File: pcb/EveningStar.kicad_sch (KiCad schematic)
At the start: 0 parts

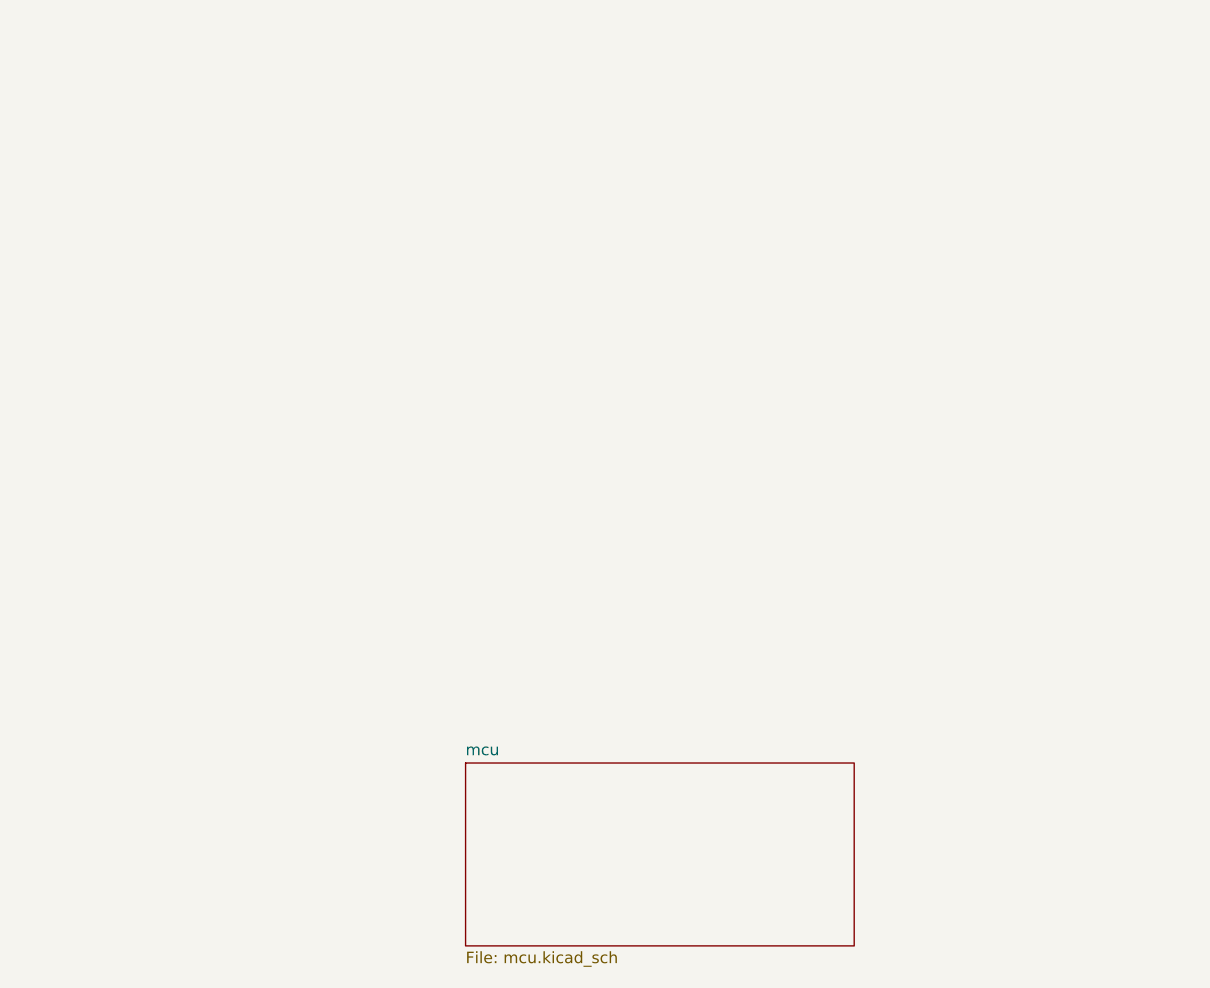
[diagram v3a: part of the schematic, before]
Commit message: feat: add W5500 ethernet controller
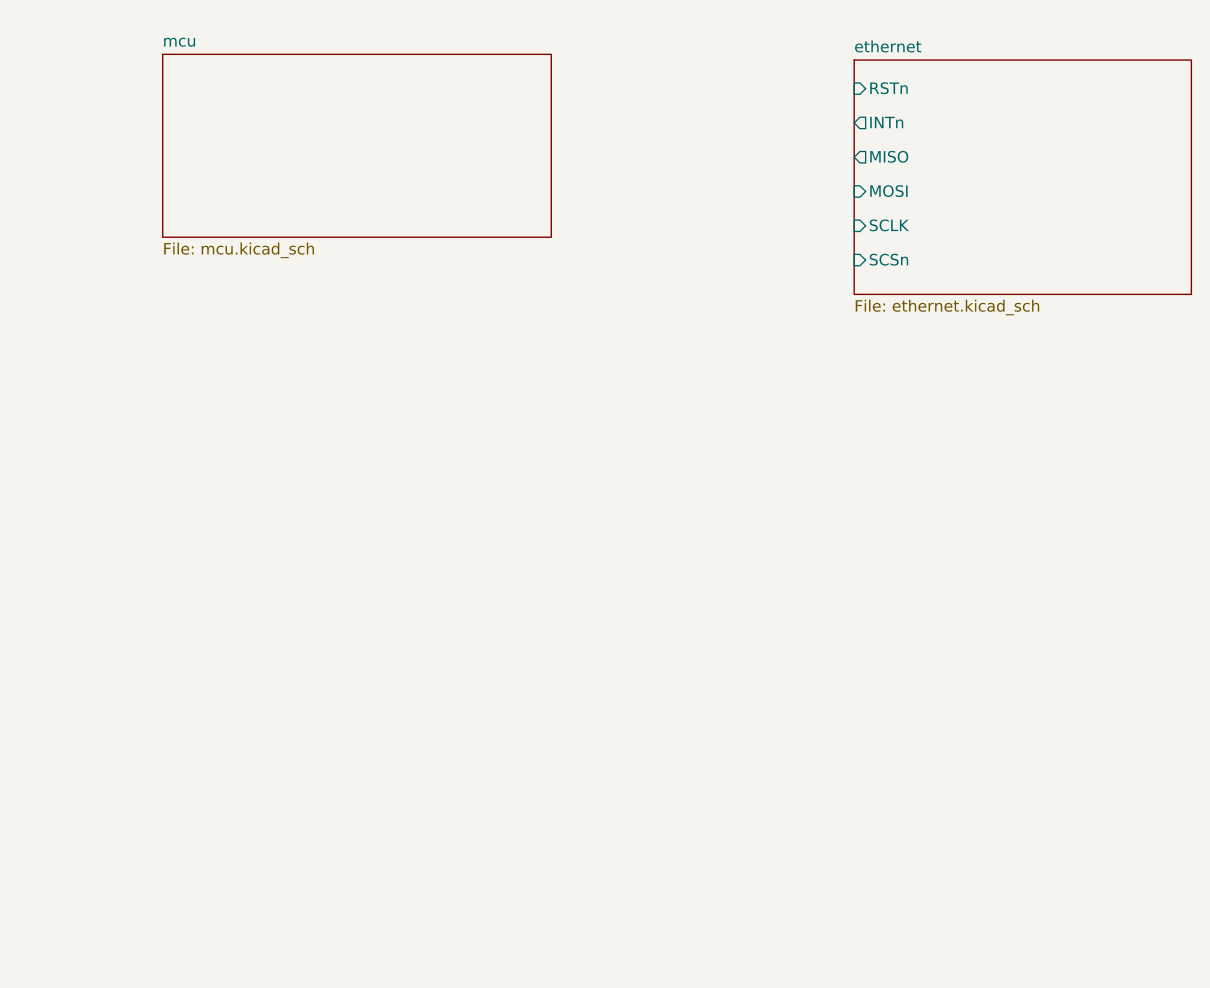
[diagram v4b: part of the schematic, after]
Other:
- added sheet ethernet (ethernet.kicad_sch)
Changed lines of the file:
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@@
 	)
 	(sheet
-		(at 134.62 116.84)
+		(at 177.8 38.735)
+		(size 37.465 26.035)
+		(exclude_from_sim no)
+		(in_bom yes)
+		(on_board yes)
+		(dnp no)
+		(fields_autoplaced yes)
+		(stroke
+			(width 0.1524)
+			(type solid)
+		)
+		(fill
+			(color 0 0 0 0)
+		)
+		(property "Sheetname" "ethernet"
+			(at 177.8 38.0234 0)
+			(show_name no)
+			(do_not_autoplace no)
+			(effects
+				(font
+					(size 1.27 1.27)
+				)
+				(justify left bottom)
+			)
+		)
+		(property "Sheetfile" "ethernet.kicad_sch"
+			(at 177.8 65.3546 0)
+			(show_name no)
+			(do_not_autoplace no)
+			(effects
+				(font
+					(size 1.27 1.27)
+				)
+				(justify left top)
+			)
+		)
+		(pin "INTn" output
+			(at 177.8 45.72 180)
+			(effects
+				(font
+					(size 1.27 1.27)
+				)
+				(justify left)
+			)
+		)
+		(pin "MISO" output
+			(at 177.8 49.53 180)
+			(effects
+				(font
+					(size 1.27 1.27)
+				)
+				(justify left)
+			)
+		)
+		(pin "MOSI" input
+			(at 177.8 53.34 180)
+			(effects
+				(font
+					(size 1.27 1.27)
+				)
+				(justify left)
+			)
+		)
+		(pin "RSTn" input
+			(at 177.8 41.91 180)
+			(effects
+				(font
+					(size 1.27 1.27)
+				)
+				(justify left)
+			)
+		)
+		(pin "SCLK" input
+			(at 177.8 57.15 180)
+			(effects
+				(font
+					(size 1.27 1.27)
+				)
+				(justify left)
+			)
+		)
+		(pin "SCSn" input
+			(at 177.8 60.96 180)
+			(effects
+				(font
+					(size 1.27 1.27)
+				)
+				(justify left)
+			)
+		)
+		(instances
+			(project "EveningStar"
+				(path "/4c61f5a2-f8d4-462a-9bc3-d74437d30372"
+					(page "5")
+				)
+			)
+		)
+	)
+	(sheet
+		(at 100.965 38.1)
 		(size 43.18 20.32)
 		(exclude_from_sim no)
@@
 		)
 		(property "Sheetname" "mcu"
-			(at 134.62 116.1284 0)
+			(at 100.965 37.3884 0)
 			(show_name no)
 			(do_not_autoplace no)
@@
 		)
 		(property "Sheetfile" "mcu.kicad_sch"
-			(at 134.62 137.7446 0)
+			(at 100.965 59.0046 0)
 			(show_name no)
 			(do_not_autoplace no)

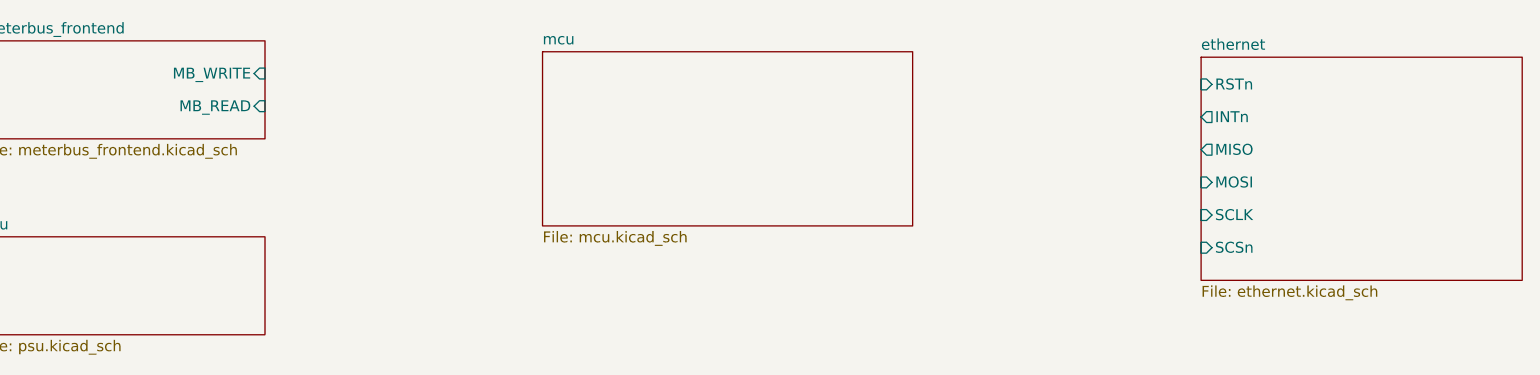
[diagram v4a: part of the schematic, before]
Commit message: feat: connect ethernet to mcu and sort erc errors
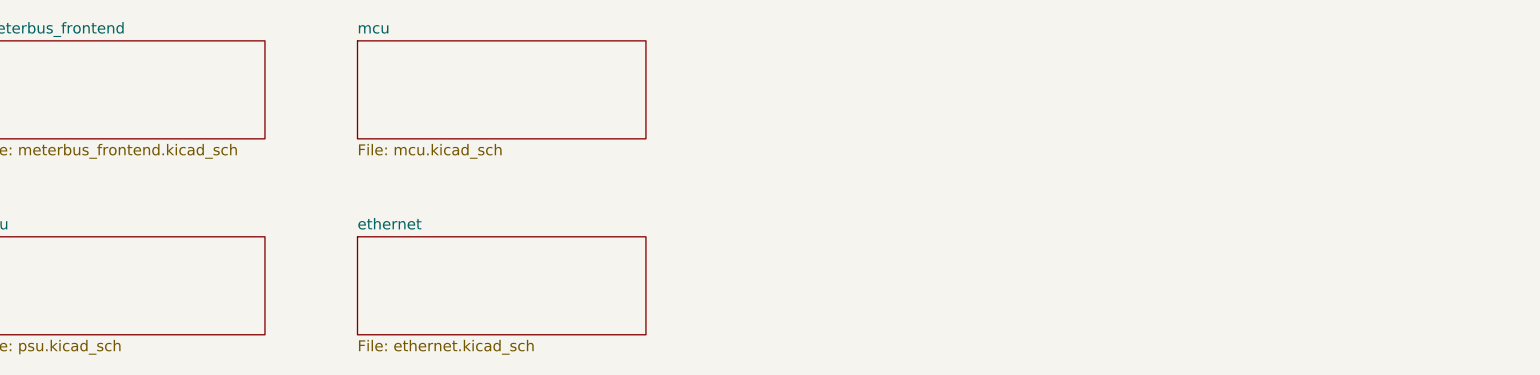
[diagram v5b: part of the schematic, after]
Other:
- sheet ethernet ports: added none; removed INTn, MISO, MOSI, RSTn, SCLK, SCSn
- sheet meterbus_frontend ports: added none; removed MB_READ, MB_WRITE
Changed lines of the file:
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@@
-			)
-		)
-		(pin "MB_READ" input
-			(at 68.58 44.45 0)
-			(effects
-				(font
-					(size 1.27 1.27)
-				)
-				(justify right)
-			)
-		)
-		(pin "MB_WRITE" input
-			(at 68.58 40.64 0)
-			(effects
-				(font
-					(size 1.27 1.27)
-				)
-				(justify right)
 			)
 		)
@@
 	)
 	(sheet
-		(at 177.8 38.735)
-		(size 37.465 26.035)
+		(at 79.375 59.69)
+		(size 33.655 11.43)
 		(exclude_from_sim no)
 		(in_bom yes)
@@
 		)
 		(property "Sheetname" "ethernet"
-			(at 177.8 38.0234 0)
+			(at 79.375 58.9784 0)
 			(show_name no)
 			(do_not_autoplace no)
@@
 		)
 		(property "Sheetfile" "ethernet.kicad_sch"
-			(at 177.8 65.3546 0)
+			(at 79.375 71.7046 0)
 			(show_name no)
 			(do_not_autoplace no)
@@
 				)
 				(justify left top)
-			)
-		)
-		(pin "INTn" output
-			(at 177.8 45.72 180)
-			(effects
-				(font
-					(size 1.27 1.27)
-				)
-				(justify left)
-			)
-		)
-		(pin "MISO" output
-			(at 177.8 49.53 180)
-			(effects
-				(font
-					(size 1.27 1.27)
-				)
-				(justify left)
-			)
-		)
-		(pin "MOSI" input
-			(at 177.8 53.34 180)
-			(effects
-				(font
-					(size 1.27 1.27)
-				)
-				(justify left)
-			)
-		)
-		(pin "RSTn" input
-			(at 177.8 41.91 180)
-			(effects
-				(font
-					(size 1.27 1.27)
-				)
-				(justify left)
-			)
-		)
-		(pin "SCLK" input
-			(at 177.8 57.15 180)
-			(effects
-				(font
-					(size 1.27 1.27)
-				)
-				(justify left)
-			)
-		)
-		(pin "SCSn" input
-			(at 177.8 60.96 180)
-			(effects
-				(font
-					(size 1.27 1.27)
-				)
-				(justify left)
 			)
 		)
@@
 	)
 	(sheet
-		(at 100.965 38.1)
-		(size 43.18 20.32)
+		(at 79.375 36.83)
+		(size 33.655 11.43)
 		(exclude_from_sim no)
 		(in_bom yes)
@@
 		)
 		(property "Sheetname" "mcu"
-			(at 100.965 37.3884 0)
+			(at 79.375 36.1184 0)
 			(show_name no)
 			(do_not_autoplace no)
@@
 		)
 		(property "Sheetfile" "mcu.kicad_sch"
-			(at 100.965 59.0046 0)
+			(at 79.375 48.8446 0)
 			(show_name no)
 			(do_not_autoplace no)

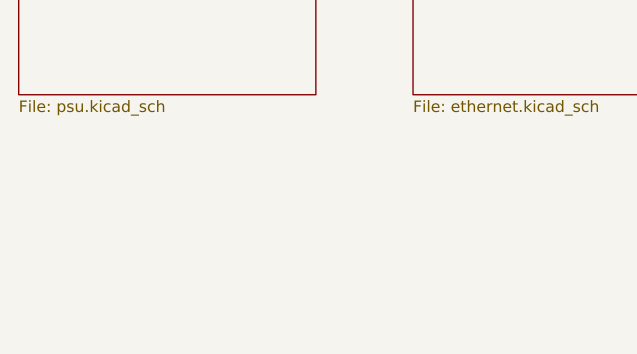
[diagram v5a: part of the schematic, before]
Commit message: feat: create pcb production files and swap some parts for basic
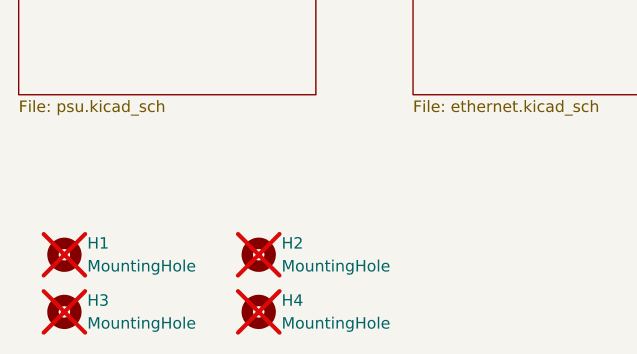
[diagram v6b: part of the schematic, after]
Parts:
- added H1, H2, H3, H4: MountingHole, EasyEDA:JLC_PCBA_Tooling_Mount, symbol Mechanical:MountingHole
